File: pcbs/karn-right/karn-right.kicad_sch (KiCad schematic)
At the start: 46 parts, among them SW11 SW_Push, SW12 SW_Push, SW13 SW_Push, SW14 SW_Push, SW15 SW_Push, SW21 SW_Push, SW22 SW_Push, SW23 SW_Push, SW24 SW_Push, SW25 SW_Push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

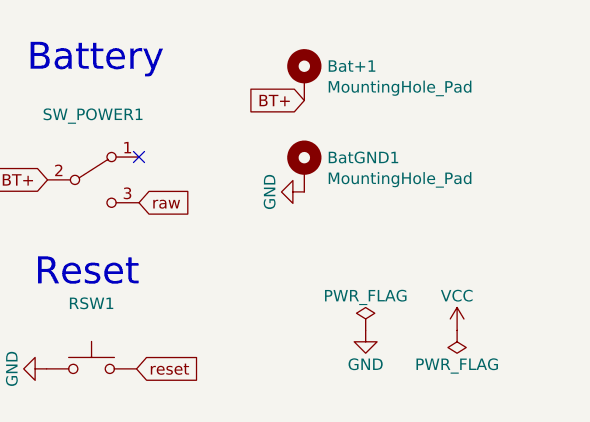
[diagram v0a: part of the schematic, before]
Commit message: Various changes:
- Add start of parts list
- Fix impossible placement of diodes
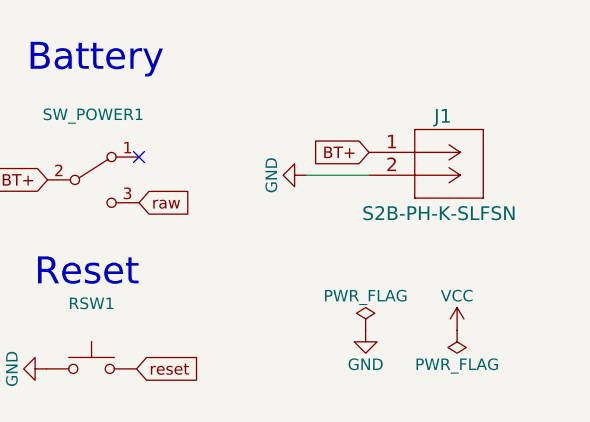
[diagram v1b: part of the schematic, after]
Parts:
- removed Bat+1, BatGND1: MountingHole_Pad, kbd:1pin_conn, symbol Mechanical:MountingHole_Pad
- added J1: S2B-PH-K-SLFSN, kbd:S2B-PH-K-SLFSN, symbol S2B-PH-K-SLFSN:S2B-PH-K-SLFSN
- SW26: footprint Button_Switch_Keyboard:MBK choc 1u -> Button_Switch_Keyboard:MBK choc 1.5u
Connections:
- net BT+: now also J1.1
- net GND: now also J1.2
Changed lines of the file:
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@@
+    (stroke (width 0) (type default) (color 0 0 0 0))
+  )
+  (wire (pts (xy 247.4891 68.2818) (xy 254.4891 68.2818))
     (stroke (width 0) (type default) (color 0 0 0 0))
   )
@@
     (effects (font (size 3 3)) (justify left bottom))
   )
-  (global_label "BT+" (shape input) (at 247.3006 59.9799 180) (fields_autoplaced)
+  (global_label "BT+" (shape input) (at 254.4891 65.7418 180) (fields_autoplaced)
     (effects (font (size 1.27 1.27)) (justify right))
-    (property "Intersheet References" "${INTERSHEET_REFS}" (id 0) (at 0.9206 18.0699 0)
+    (property "Intersheet References" "${INTERSHEET_REFS}" (id 0) (at 8.1091 23.8318 0)
       (effects (font (size 1.27 1.27)) hide)
     )
@@
       (effects (font (size 1.27 1.27)) hide)
     )
-    (property "Footprint" "Button_Switch_Keyboard:MBK choc 1u" (id 2) (at 126.5261 78.6582 0)
+    (property "Footprint" "Button_Switch_Keyboard:MBK choc 1.5u" (id 2) (at 126.5261 78.6582 0)
       (effects (font (size 1.27 1.27)) hide)
     )
@@
     (pin "2")
   )
-  (symbol (lib_id "Mechanical:MountingHole_Pad") (at 247.3006 67.5999 0) (unit 1)
-    (in_bom yes) (on_board yes)
-    (property "Reference" "BatGND1" (id 0) (at 249.8406 66.3553 0)
-      (effects (font (size 1.27 1.27)) (justify left))
-    )
-    (property "Value" "MountingHole_Pad" (id 1) (at 249.8406 68.6667 0)
-      (effects (font (size 1.27 1.27)) (justify left))
-    )
-    (property "Footprint" "kbd:1pin_conn" (id 2) (at 247.3006 67.5999 0)
-      (effects (font (size 1.27 1.27)) hide)
-    )
-    (property "Datasheet" "~" (id 3) (at 247.3006 67.5999 0)
-      (effects (font (size 1.27 1.27)) hide)
-    )
-    (pin "1")
-  )
   (symbol (lib_name "SW_Push_2") (lib_id "Switch:SW_Push") (at 48.5261 66.6582 0) (unit 1)
     (in_bom yes) (on_board yes)
@@
     (pin "2")
   )
-  (symbol (lib_id "power:GND") (at 247.3006 70.1399 270) (unit 1)
-    (in_bom yes) (on_board yes)
-    (property "Reference" "#PWR07" (id 0) (at 240.9506 70.1399 0)
-      (effects (font (size 1.27 1.27)) hide)
-    )
-    (property "Value" "GND" (id 1) (at 243.4906 70.1399 0))
-    (property "Footprint" "" (id 2) (at 247.3006 70.1399 0)
-      (effects (font (size 1.27 1.27)) hide)
-    )
-    (property "Datasheet" "" (id 3) (at 247.3006 70.1399 0)
-      (effects (font (size 1.27 1.27)) hide)
-    )
-    (pin "1")
+  (symbol (lib_id "power:GND") (at 247.4891 68.2818 270) (unit 1)
+    (in_bom yes) (on_board yes)
+    (property "Reference" "#PWR07" (id 0) (at 241.1391 68.2818 0)
+      (effects (font (size 1.27 1.27)) hide)
+    )
+    (property "Value" "GND" (id 1) (at 243.6791 68.2818 0))
+    (property "Footprint" "" (id 2) (at 247.4891 68.2818 0)
+      (effects (font (size 1.27 1.27)) hide)
+    )
+    (property "Datasheet" "" (id 3) (at 247.4891 68.2818 0)
+      (effects (font (size 1.27 1.27)) hide)
+    )
+    (pin "1")
+  )
+  (symbol (lib_id "S2B-PH-K-SLFSN:S2B-PH-K-SLFSN") (at 254.4891 65.7418 0) (unit 1)
+    (in_bom yes) (on_board yes)
+    (property "Reference" "J1" (id 0) (at 261.7204 61.7418 0)
+      (effects (font (size 1.524 1.524)) (justify left))
+    )
+    (property "Value" "S2B-PH-K-SLFSN" (id 1) (at 253.7204 72.5518 0)
+      (effects (font (size 1.524 1.524)) (justify left))
+    )
+    (property "Footprint" "kbd:S2B-PH-K-SLFSN" (id 2) (at 264.6491 67.2658 0)
+      (effects (font (size 1.524 1.524)) hide)
+    )
+    (property "Datasheet" "" (id 3) (at 254.4891 65.7418 0)
+      (effects (font (size 1.524 1.524)) hide)
+    )
+    (pin "1")
+    (pin "2")
   )
   (symbol (lib_name "SW_Push_4") (lib_id "Switch:SW_Push") (at 48.5261 127.6582 0) (unit 1)
@@
     (pin "2")
   )
-  (symbol (lib_id "Mechanical:MountingHole_Pad") (at 247.3006 57.4399 0) (unit 1)
-    (in_bom yes) (on_board yes)
-    (property "Reference" "Bat+1" (id 0) (at 249.8406 56.1953 0)
-      (effects (font (size 1.27 1.27)) (justify left))
-    )
-    (property "Value" "MountingHole_Pad" (id 1) (at 249.8406 58.5067 0)
-      (effects (font (size 1.27 1.27)) (justify left))
-    )
-    (property "Footprint" "kbd:1pin_conn" (id 2) (at 247.3006 57.4399 0)
-      (effects (font (size 1.27 1.27)) hide)
-    )
-    (property "Datasheet" "~" (id 3) (at 247.3006 57.4399 0)
-      (effects (font (size 1.27 1.27)) hide)
-    )
-    (pin "1")
-  )
   (symbol (lib_id "power:GND") (at 254.1144 85.5213 0) (unit 1)
     (in_bom yes) (on_board yes)
@@
       (reference "#PWR09") (unit 1) (value "VCC") (footprint "")
     )
-    (path "/efb65c8e-3384-448c-b678-266856c0d8f6"
-      (reference "Bat+1") (unit 1) (value "MountingHole_Pad") (footprint "kbd:1pin_conn")
-    )
-    (path "/561a1ee9-d5de-461f-880e-6b93ad58e431"
-      (reference "BatGND1") (unit 1) (value "MountingHole_Pad") (footprint "kbd:1pin_conn")
-    )
     (path "/817acd3d-65d5-4d98-84f9-5556e4094c7a"
       (reference "D11") (unit 1) (value "D") (footprint "Diode_SMD:1N4148X-TP")
@@
       (reference "D43") (unit 1) (value "D") (footprint "Diode_SMD:1N4148X-TP")
     )
+    (path "/a53ef69a-8078-4623-9cd4-3672c42f5863"
+      (reference "J1") (unit 1) (value "S2B-PH-K-SLFSN") (footprint "kbd:S2B-PH-K-SLFSN")
+    )
     (path "/7f9c7077-7594-446f-ae61-381d3d9fb6cc"
       (reference "L1") (unit 1) (value "SK6812MINI") (footprint "LED_SMD:LED_SK6812MINI_PLCC4_3.5x3.5mm_P1.75mm")
@@
     )
     (path "/25e4626f-10cc-4070-9cb9-2574a33a5125"
-      (reference "SW26") (unit 1) (value "SW_Push") (footprint "Button_Switch_Keyboard:MBK choc 1u")
+      (reference "SW26") (unit 1) (value "SW_Push") (footprint "Button_Switch_Keyboard:MBK choc 1.5u")
     )
     (path "/ff2a0c34-dd38-42f5-89c0-4957aab6bd1b"

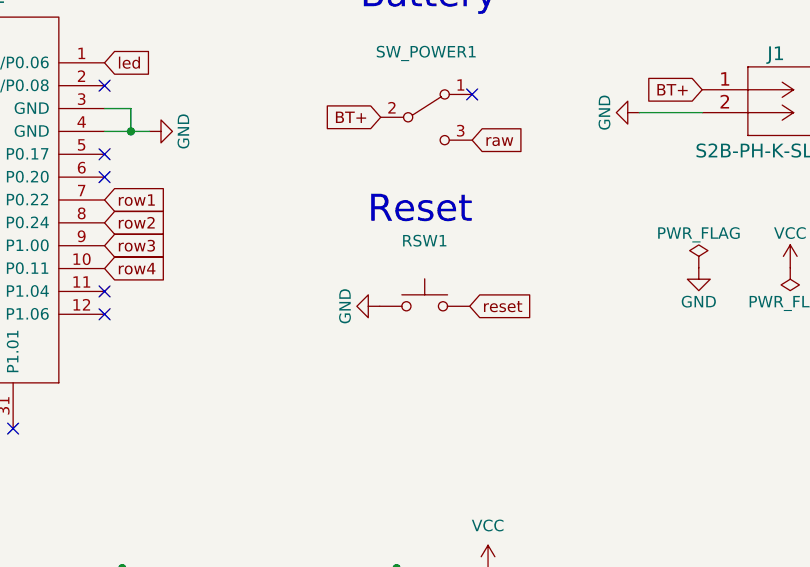
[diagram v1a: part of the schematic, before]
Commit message: karn-right v1 with gerber files
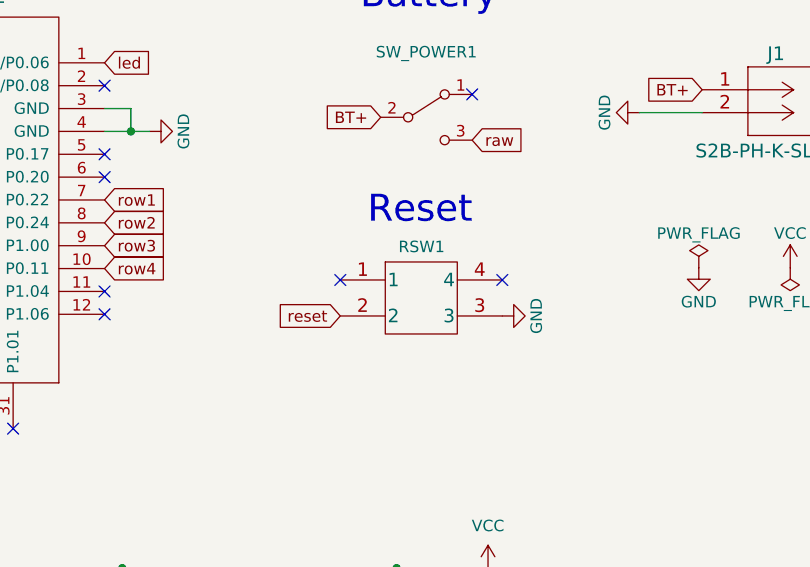
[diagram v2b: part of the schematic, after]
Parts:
- RSW1: footprint kbd:ResetSW -> karn-kicad-footprints:reset-switch-TL3313AF250QG; symbol Switch:SW_Push -> reset-switch-TL3313AF250QG:TL3313AF250QG
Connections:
- net GND: now also RSW1.3; no longer RSW1.1
- no-connect marks 12 -> 14
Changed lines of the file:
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@@
   (no_connect (at 188.0872 72.9089))
   (no_connect (at 174.1172 103.3889))
+  (no_connect (at 214.2785 86.8773))
   (no_connect (at 228.9292 66.2603))
+  (no_connect (at 232.2785 86.8773))
   (no_connect (at 149.4142 122.0727))
   (no_connect (at 152.5272 90.6889))
@@
     )
   )
-  (global_label "reset" (shape input) (at 228.6577 89.7988 0) (fields_autoplaced)
-    (effects (font (size 1.27 1.27)) (justify left))
-    (property "Intersheet References" "${INTERSHEET_REFS}" (id 0) (at 101.6577 50.4288 0)
+  (global_label "reset" (shape input) (at 214.2785 90.8773 180) (fields_autoplaced)
+    (effects (font (size 1.27 1.27)) (justify right))
+    (property "Intersheet References" "${INTERSHEET_REFS}" (id 0) (at 341.2785 130.2473 0)
       (effects (font (size 1.27 1.27)) hide)
     )
@@
     (pin "2")
   )
-  (symbol (lib_id "Switch:SW_Push") (at 223.6577 89.7988 0) (unit 1)
-    (in_bom yes) (on_board yes)
-    (property "Reference" "RSW1" (id 0) (at 223.6577 82.5598 0))
-    (property "Value" "SW_Push" (id 1) (at 223.6577 84.8712 0)
-      (effects (font (size 1.27 1.27)) hide)
-    )
-    (property "Footprint" "kbd:ResetSW" (id 2) (at 223.6577 84.7188 0)
-      (effects (font (size 1.27 1.27)) hide)
-    )
-    (property "Datasheet" "~" (id 3) (at 223.6577 84.7188 0)
-      (effects (font (size 1.27 1.27)) hide)
-    )
-    (pin "1")
-    (pin "2")
+  (symbol (lib_id "reset-switch-TL3313AF250QG:TL3313AF250QG") (at 223.2785 88.8773 0) (unit 1)
+    (in_bom yes) (on_board yes)
+    (property "Reference" "RSW1" (id 0) (at 223.3112 83.1945 0))
+    (property "Value" "SW_Push" (id 1) (at 223.2785 80.8773 0)
+      (effects (font (size 1.27 1.27)) hide)
+    )
+    (property "Footprint" "karn-kicad-footprints:reset-switch-TL3313AF250QG" (id 2) (at 223.2785 94.8773 0)
+      (effects (font (size 1.524 1.524)) hide)
+    )
+    (property "Datasheet" "~" (id 3) (at 223.2785 88.8773 0)
+      (effects (font (size 1.524 1.524)) hide)
+    )
+    (pin "1")
+    (pin "2")
+    (pin "3")
+    (pin "4")
   )
   (symbol (lib_name "SW_Push_8") (lib_id "Switch:SW_Push") (at 109.5261 106.6582 0) (unit 1)
@@
     (pin "2")
   )
-  (symbol (lib_id "power:GND") (at 218.6577 89.7988 270) (unit 1)
-    (in_bom yes) (on_board yes)
-    (property "Reference" "#PWR05" (id 0) (at 212.3077 89.7988 0)
-      (effects (font (size 1.27 1.27)) hide)
-    )
-    (property "Value" "GND" (id 1) (at 214.8477 89.7988 0))
-    (property "Footprint" "" (id 2) (at 218.6577 89.7988 0)
-      (effects (font (size 1.27 1.27)) hide)
-    )
-    (property "Datasheet" "" (id 3) (at 218.6577 89.7988 0)
+  (symbol (lib_id "power:GND") (at 232.2785 90.8773 90) (unit 1)
+    (in_bom yes) (on_board yes)
+    (property "Reference" "#PWR05" (id 0) (at 238.6285 90.8773 0)
+      (effects (font (size 1.27 1.27)) hide)
+    )
+    (property "Value" "GND" (id 1) (at 236.0885 90.8773 0))
+    (property "Footprint" "" (id 2) (at 232.2785 90.8773 0)
+      (effects (font (size 1.27 1.27)) hide)
+    )
+    (property "Datasheet" "" (id 3) (at 232.2785 90.8773 0)
       (effects (font (size 1.27 1.27)) hide)
     )
@@
     )
     (path "/0eece0c9-6947-4883-a87e-b445b80630d9"
-      (reference "RSW1") (unit 1) (value "SW_Push") (footprint "kbd:ResetSW")
+      (reference "RSW1") (unit 1) (value "SW_Push") (footprint "karn-kicad-footprints:reset-switch-TL3313AF250QG")
     )
     (path "/60c85a9c-c0d2-4469-b84c-2eacd924bd6c"
